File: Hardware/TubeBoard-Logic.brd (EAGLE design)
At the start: 63.5 x 67 mm, 30 parts, among them IC1 74HC373DW, IC2 74HC373DW, IC3 74HC85D, IC4 74HC08D, IC5 74HC04D, IC6 MKE04Z8, J1 CORTEX_DEBUG_PTH

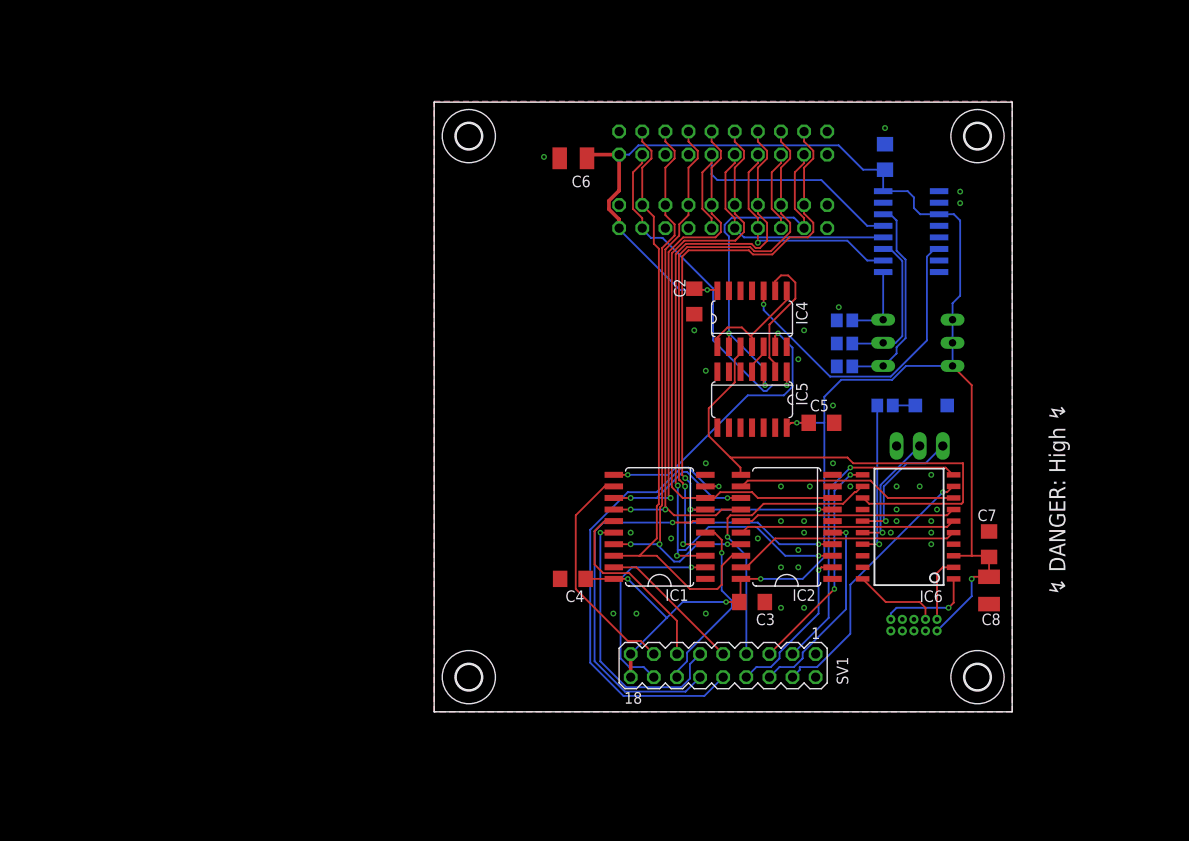
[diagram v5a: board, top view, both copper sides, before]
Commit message: more work for vfd command handling
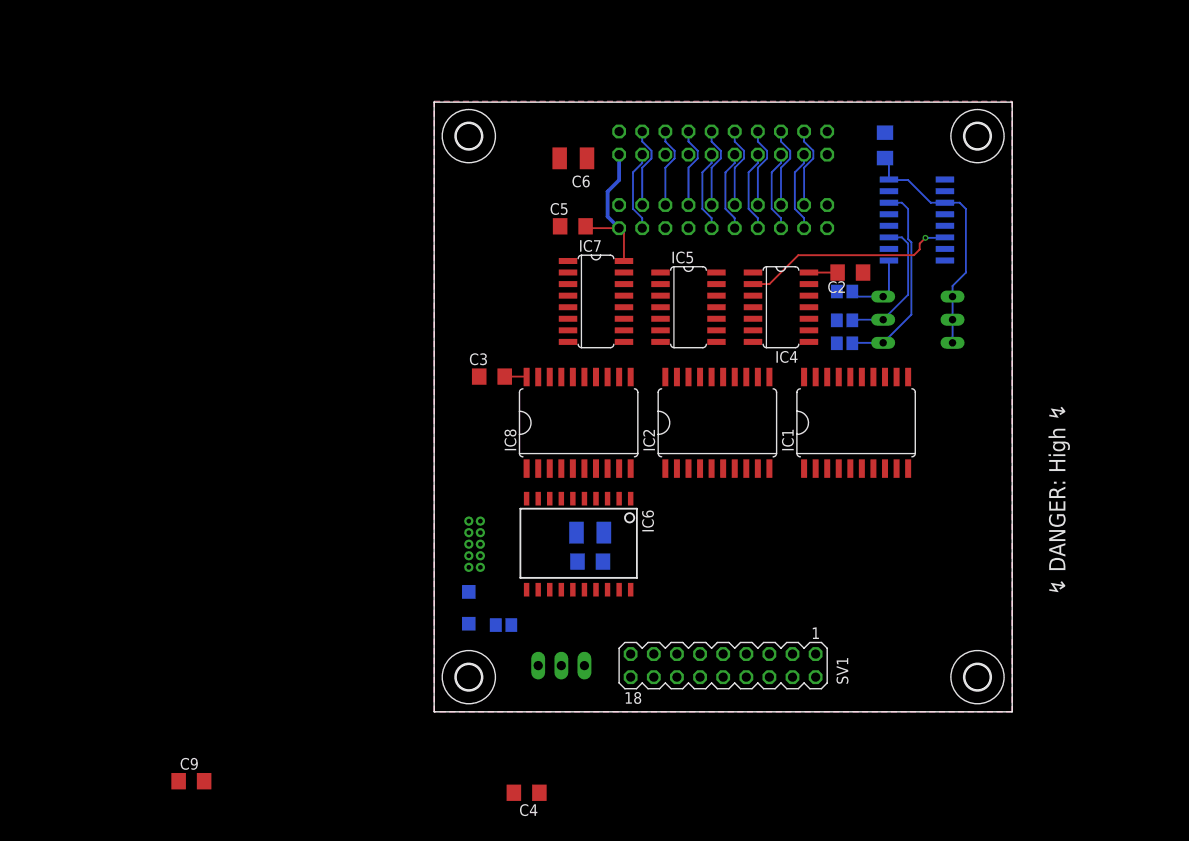
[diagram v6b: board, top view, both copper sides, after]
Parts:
- added C9: 100nF, rcl:C1206
- added IC7: 74HC139D, 74xx-eu:SO16
- added IC8: 74HC373DW, 74xx-eu:SO20W
- moved LED1 55.4 mm to (3.81, 11.4), turned to 0 degrees
- moved J1 49.1 mm to (4.45, 18.4), turned to 90 degrees
- moved R4 48.4 mm to (7.62, 9.53), turned to 0 degrees
- moved SV4 46.2 mm to (14.0, 5.08), turned to 0 degrees
- moved C8 44.3 mm to (17.1, 19.7), flipped to the bottom, turned to 0 degrees
- moved C7 43.9 mm to (17.1, 16.5), flipped to the bottom, turned to 0 degrees
- moved C3 37.8 mm to (6.35, 36.8), turned to 180 degrees
- moved IC6 36.2 mm to (15.9, 18.4), turned to 180 degrees
- moved C5 34.8 mm to (15.2, 53.3), turned to 180 degrees
- moved WEED1 31.3 mm to (-12.7, 51.4)
- moved IC1 24.4 mm to (46.4, 31.8), turned to 0 degrees
- moved C4 24.0 mm to (10.2, -8.89)
- moved C2 17.4 mm to (45.7, 48.3), turned to 0 degrees
- moved IC2 13.7 mm to (31.1, 31.8), turned to 0 degrees
- moved IC5 12.3 mm to (27.9, 44.5), turned to 270 degrees
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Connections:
- removed net !A0: IC4.5, IC5.4
- removed net DRIVE0: IC2.12, IC6.8
- removed net DRIVE1: IC2.15, IC6.7
- removed net DRIVE2: IC2.16, IC6.6
- removed net DRIVE3: IC2.19, IC6.5
- new net !BOARD_SELECT: IC5.2, IC7.1
- new net !CONTROL_LATCH: IC5.5, IC7.5
- new net !DIGIT_LATCH: IC5.3, IC7.4
- new net !PWM_LATCH: IC5.9, IC7.6
- new net PWM_D0: IC6.8, IC8.2
- new net PWM_D1: IC6.7, IC8.5
- new net PWM_D2: IC6.6, IC8.6
- new net PWM_D3: IC6.5, IC8.9
- new net PWM_LATCH: IC5.8, IC6.13, IC8.11
- net !NIXIE_CS: now also IC5.11; no longer IC5.1
- net +5V: now also C9.1, IC7.16, IC8.20
- net A0: now also IC7.2; no longer IC4.2, IC5.3
- net A1: now also IC7.3
- net BOARD_SELECT: now also IC4.3, IC5.1; no longer IC4.1, IC4.4, IC4.8
- net CONTROL_LATCH: now also IC5.6; no longer IC4.3, IC6.13
- net D0: now also IC8.3
- net D1: now also IC8.4
- net D2: now also IC8.7
- net D3: now also IC8.8
- net D4: now also IC8.13
- net D5: now also IC8.14
- net D6: now also IC8.17
- net D7: now also IC8.18
- net DIGIT_LATCH: now also IC5.4; no longer IC4.6
- net GND: now also C9.2, IC4.10, IC4.4, IC4.5, IC4.9, IC7.8, IC8.1, IC8.10; no longer IC5.11, IC5.5, IC5.9
- net NIXIE_CS: now also IC4.1, IC5.10; no longer IC4.9, IC5.2
- net SELECT_EN: now also IC4.2; no longer IC4.10
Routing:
- net +5V: track 204.6 -> 50.1 mm, vias 6 -> 0
- net D0: track 80.1 -> 8.92 mm, vias 3 -> 0
- net D1: track 77.8 -> 8.92 mm, vias 3 -> 0
- net D2: track 73.6 -> 8.92 mm, vias 3 -> 0
- net CONTROL_LATCH: track 58.5 -> 0.00 mm
- net D7: track 67.3 -> 8.92 mm
- net D3: track 65.6 -> 8.92 mm
- net D4: track 63.9 -> 8.92 mm, vias 3 -> 0
- net D6: track 63.2 -> 8.92 mm, vias 3 -> 0
- net LDIGIT3: track 50.9 -> 0.00 mm, vias 1 -> 0
- net D5: track 58.1 -> 8.92 mm, vias 2 -> 0
- net LDIGIT2: track 40.5 -> 0.00 mm, vias 1 -> 0
- net PWM2: track 34.8 -> 0.00 mm, vias 1 -> 0
- net PWM0: track 32.1 -> 0.00 mm, vias 1 -> 0
- net A0: track 41.0 -> 8.92 mm, vias 2 -> 0
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
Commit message: more routing of tube logic board
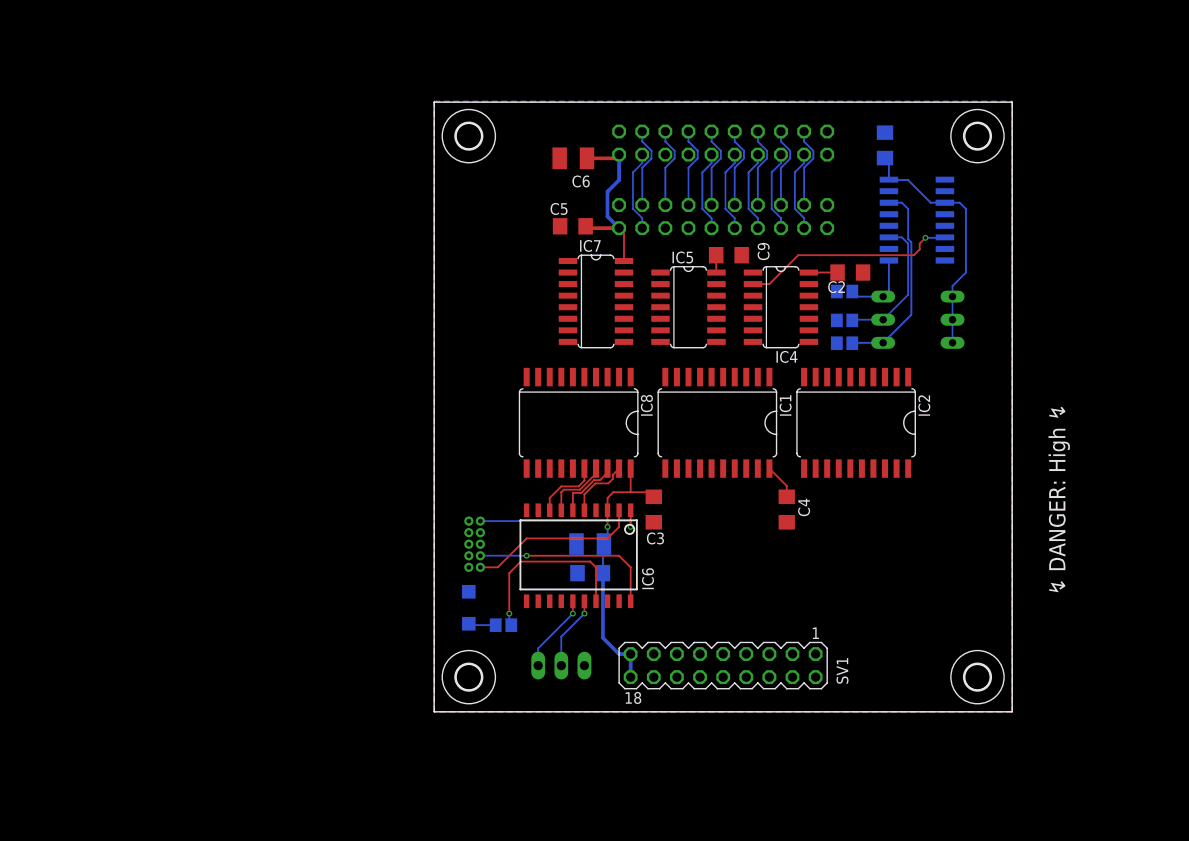
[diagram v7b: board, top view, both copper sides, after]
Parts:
- IC1, IC2, IC8: value 74HC373DW -> 74HC573D
- moved C9 82.6 mm to (32.4, 50.2)
- moved C4 42.2 mm to (38.7, 22.2), turned to 270 degrees
- moved C3 23.0 mm to (24.1, 22.2), turned to 270 degrees
- moved IC1 15.2 mm to (31.1, 31.8), turned to 180 degrees
- moved IC2 15.2 mm to (46.4, 31.8), turned to 180 degrees
- moved C7 1.27 mm to (17.1, 15.2)
- moved C8 1.27 mm to (17.1, 18.4)
- moved IC6 1.27 mm to (15.9, 17.1)
- turned IC8 to 180 degrees
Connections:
- net COLON_B: now also IC2.19; no longer IC2.2
- net COLON_T: now also IC2.18; no longer IC2.5
- net CONTROL_LATCH: now also IC2.1; no longer IC2.11
- net D0: now also IC1.2, IC2.2, IC8.2; no longer IC1.3, IC2.3, IC8.3
- net D1: now also IC1.3, IC2.3, IC8.3; no longer IC1.4, IC2.4, IC8.4
- net D2: now also IC1.4, IC2.4, IC8.4; no longer IC1.7, IC2.7, IC8.7
- net D3: now also IC1.5, IC2.5, IC8.5; no longer IC1.8, IC2.8, IC8.8
- net D4: now also IC1.6, IC2.6, IC8.6; no longer IC1.13, IC2.13, IC8.13
- net D5: now also IC1.7, IC2.7, IC8.7; no longer IC1.14, IC2.14, IC8.14
- net D6: now also IC1.8, IC2.8, IC8.8; no longer IC1.17, IC2.17, IC8.17
- net D7: now also IC1.9, IC2.9, IC8.9; no longer IC1.18, IC2.18, IC8.18
- net DIGIT_LATCH: now also IC1.1; no longer IC1.11
- net GND: now also IC1.11, IC2.11, IC8.11; no longer IC1.1, IC2.1, IC8.1
- net LDIGIT0: now also IC1.19; no longer IC1.2
- net LDIGIT1: now also IC1.18; no longer IC1.5
- net LDIGIT2: now also IC1.17; no longer IC1.6
- net LDIGIT3: now also IC1.16; no longer IC1.9
- net PWM_D0: now also IC6.5, IC8.19; no longer IC6.8, IC8.2
- net PWM_D1: now also IC6.6, IC8.18; no longer IC6.7, IC8.5
- net PWM_D2: now also IC6.7, IC8.17; no longer IC6.6, IC8.6
- net PWM_D3: now also IC6.8, IC8.16; no longer IC6.5, IC8.9
- net PWM_LATCH: now also IC8.1; no longer IC8.11
- net RDIGIT0: now also IC1.15; no longer IC1.12
- net RDIGIT1: now also IC1.14; no longer IC1.15
- net RDIGIT2: now also IC1.13; no longer IC1.16
- net RDIGIT3: now also IC1.12; no longer IC1.19
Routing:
- net +5V: track 50.1 -> 87.9 mm, vias 0 -> 1
- net ARM_SWDCLK: track 0.00 -> 20.8 mm, vias 0 -> 1
- net STATUS0: track 0.00 -> 19.8 mm, vias 0 -> 1
- net !ARM_RESET: track 0.00 -> 19.0 mm, vias 0 -> 1
- net ARM_SWDIO: track 0.00 -> 18.9 mm
- net UART_TX: track 0.00 -> 8.64 mm, vias 0 -> 1
- net UART_RX: track 0.00 -> 8.12 mm, vias 0 -> 1
- net PWM_D2: track 0.00 -> 7.39 mm
- net PWM_D3: track 0.00 -> 7.27 mm
- net PWM_D1: track 0.00 -> 7.23 mm
- net PWM_D0: track 0.00 -> 6.98 mm
- net N$9: track 0.00 -> 3.02 mm

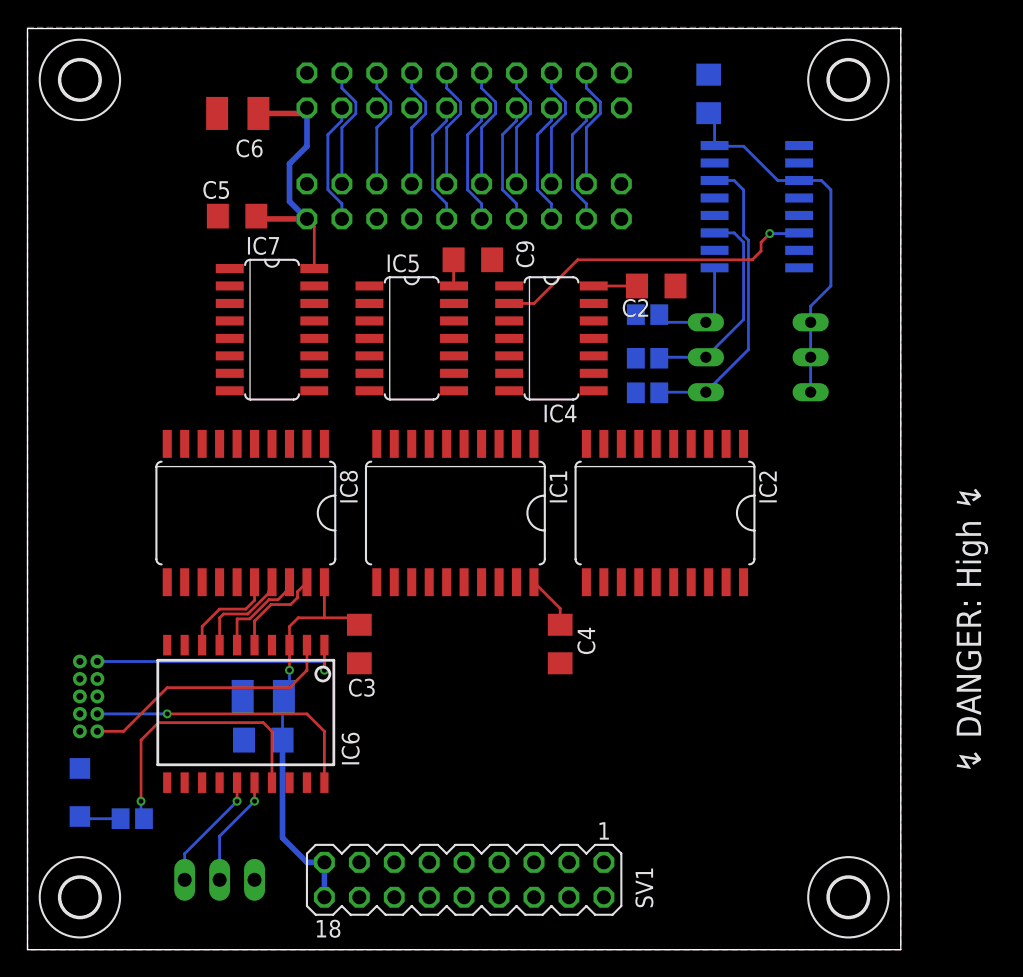
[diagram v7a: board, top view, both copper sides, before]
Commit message: finished routing basic data latch only tube logic board
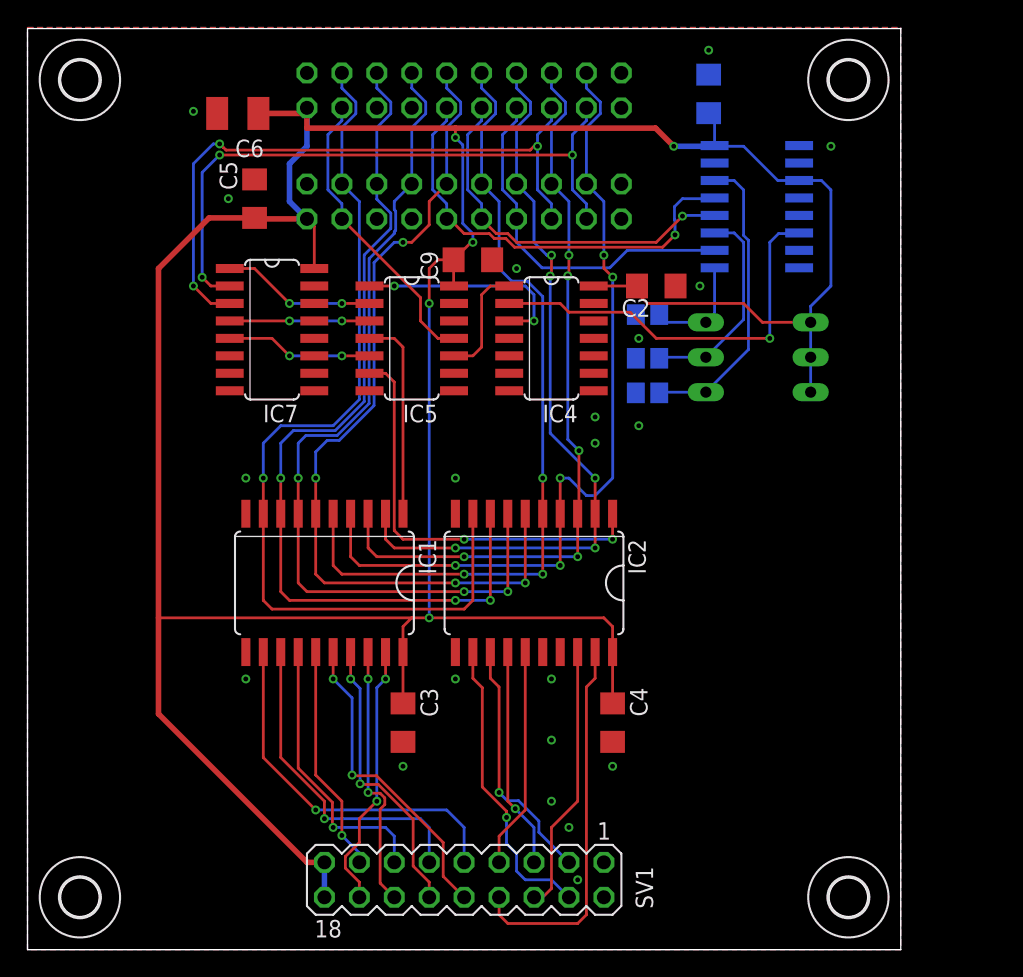
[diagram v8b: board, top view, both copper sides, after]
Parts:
- removed C7: 100nF, rcl:C1206
- removed C8: 10µF, rcl:SMC_B
- removed IC6: MKE04Z8, Parts:SOIC20S
- removed IC8: 74HC573D, 74xx-eu:SO20W
- removed J1: CORTEX_DEBUG_PTH, SparkFun-Connectors:2X5-PTH-1.27MM
- removed LED1: (no value), led:CHIPLED_1206
- removed R4: 3k, rcl:R2012
- removed SV4: (no value), con-lstb:MA03-1
- moved WEED1 74.7 mm to (57.8, 26.7)
- moved IC1 10.8 mm to (21.6, 26.7)
- moved IC2 10.8 mm to (36.8, 26.7)
- moved C4 6.87 mm to (42.5, 16.5)
- moved C3 6.54 mm to (27.3, 16.5)
- moved C5 1.80 mm to (16.5, 54.6), turned to 90 degrees
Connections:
- removed net !ARM_RESET: IC6.1, J1.10
- removed net !PWM_LATCH: IC5.9, IC7.6
- removed net ARM_SWDCLK: IC6.20, J1.4
- removed net ARM_SWDIO: IC6.2, J1.2
- removed net N$9: LED1.A, R4.2
- removed net PWM_D0: IC6.5, IC8.19
- removed net PWM_D1: IC6.6, IC8.18
- removed net PWM_D2: IC6.7, IC8.17
- removed net PWM_D3: IC6.8, IC8.16
- removed net PWM_LATCH: IC5.8, IC6.13, IC8.1
- removed net STATUS0: IC6.17, R4.1
- removed net UART_RX: IC6.16, SV4.2
- removed net UART_TX: IC6.15, SV4.3
- net +5V: no longer C7.1, C8.+, IC6.3, IC8.20, J1.1
- net D0: no longer IC8.2
- net D1: no longer IC8.3
- net D2: no longer IC8.4
- net D3: no longer IC8.5
- net D4: no longer IC8.6
- net D5: no longer IC8.7
- net D6: no longer IC8.8
- net D7: no longer IC8.9
- net GND: now also IC5.9; no longer C7.2, C8.-, IC6.4, IC8.10, IC8.11, J1.3, J1.5, J1.9, LED1.C, SV4.1
- net PWM0: now also IC2.15; no longer IC6.12
- net PWM1: now also IC2.14; no longer IC6.11
- net PWM2: now also IC2.13; no longer IC6.10
- net PWM3: now also IC2.12; no longer IC6.9
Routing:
- net +5V: track 87.9 -> 242.4 mm, vias 1 -> 5
- net D7: track 8.92 -> 66.9 mm, vias 0 -> 1
- net D6: track 8.92 -> 65.9 mm, vias 0 -> 3
- net D5: track 8.92 -> 63.9 mm, vias 0 -> 3
- net D4: track 8.92 -> 63.0 mm, vias 0 -> 4
- net D2: track 8.92 -> 60.9 mm, vias 0 -> 5
- net D3: track 8.92 -> 59.1 mm, vias 0 -> 3
- net D0: track 8.92 -> 55.4 mm, vias 0 -> 5
- net D1: track 8.92 -> 54.9 mm, vias 0 -> 5
- net A1: track 8.92 -> 46.9 mm, vias 0 -> 3
- net A0: track 8.92 -> 46.3 mm, vias 0 -> 3
- net CONTROL_LATCH: track 0.00 -> 30.9 mm, vias 0 -> 2
- net COLON_B: track 0.00 -> 27.5 mm
- net RDIGIT3: track 0.00 -> 26.9 mm, vias 0 -> 1
- net RDIGIT2: track 0.00 -> 23.9 mm, vias 0 -> 1
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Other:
- board text removed: "↯ DANGER: High ↯"
